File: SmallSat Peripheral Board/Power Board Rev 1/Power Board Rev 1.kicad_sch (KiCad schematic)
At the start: 41 parts, among them J1 Conn_01x02_Pin, J2 Conn_01x02_Pin, U1 DMN3020UFDF, U2 BQ296202DSGR, U3 DMN3020UFDF, U4 BQ28Z620DRZR, U5 TPS62993QRYTRQ1, U6 TPS62993QRYTRQ1

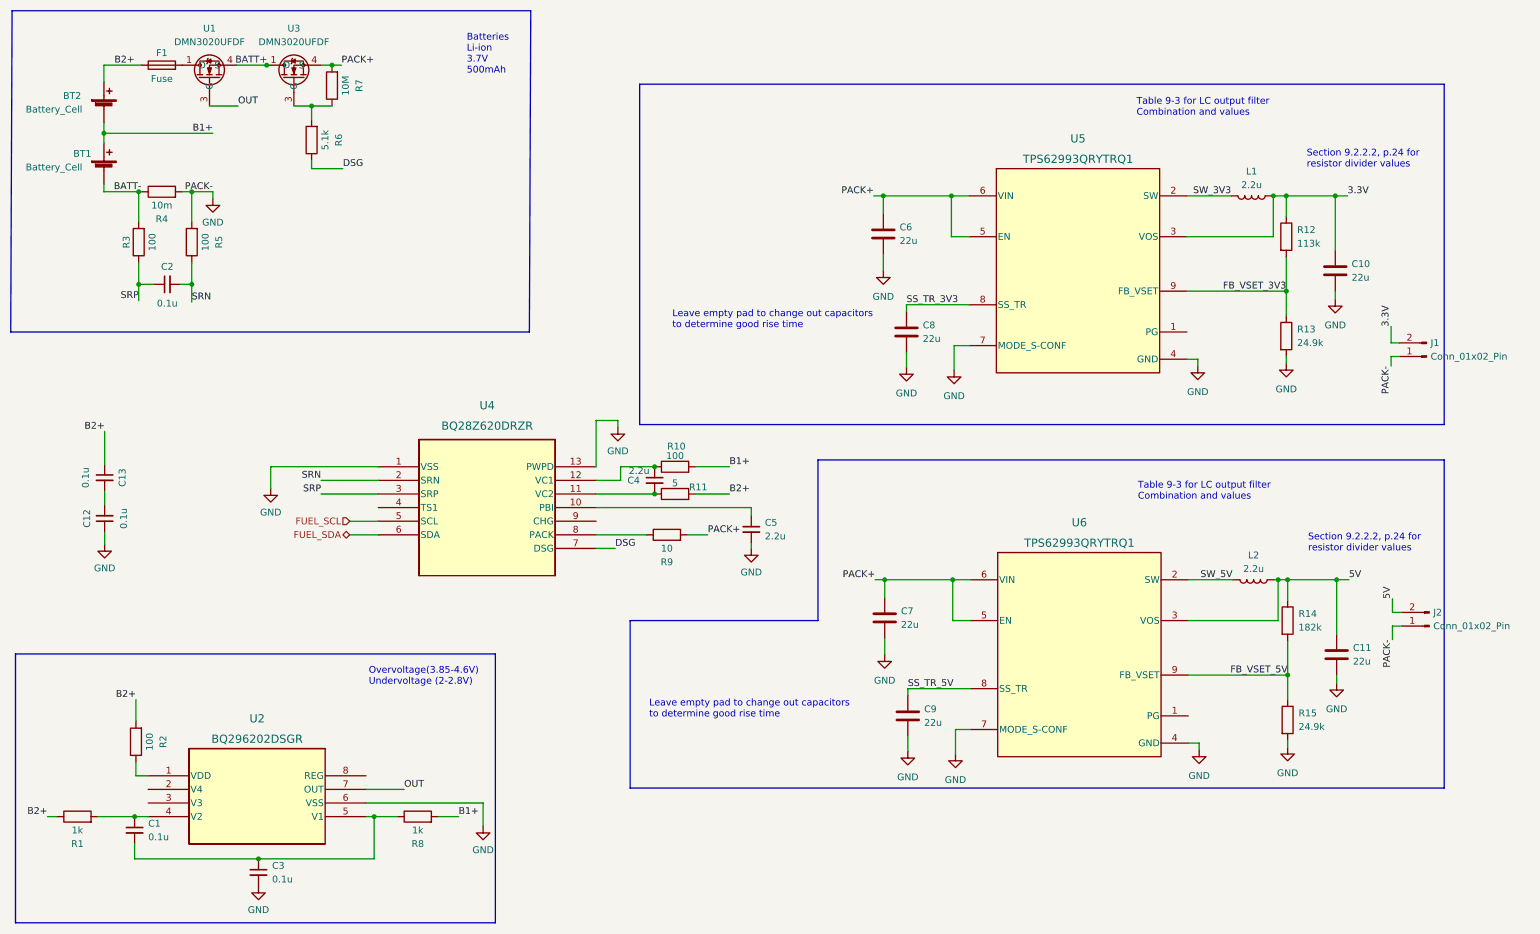
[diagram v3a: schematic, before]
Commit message: Power Board Rev 1 Gerber Files Generated
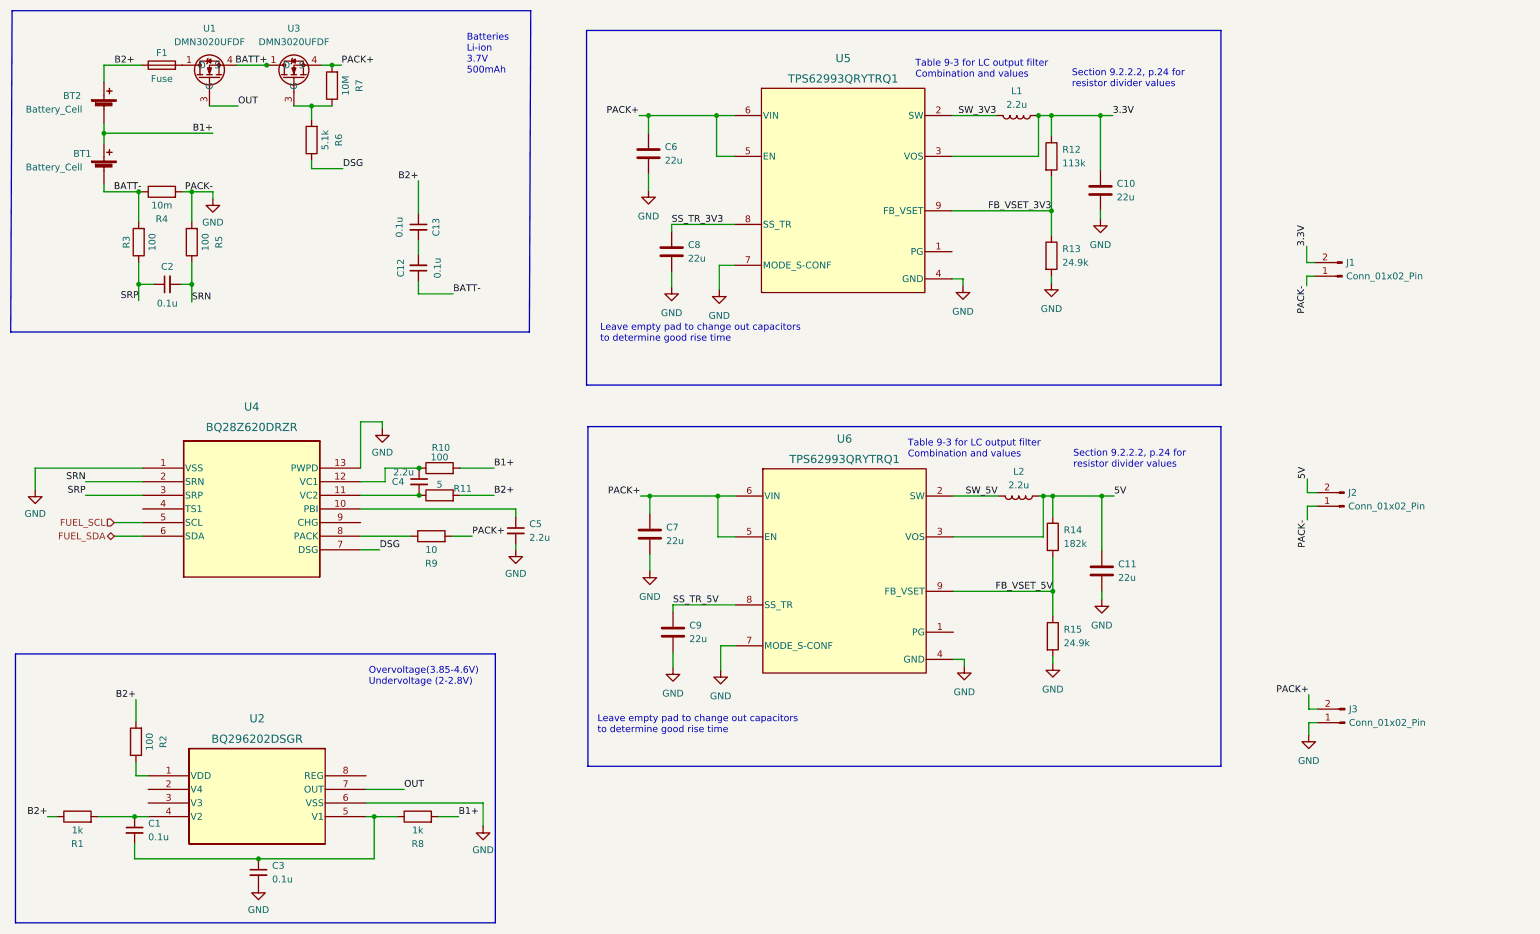
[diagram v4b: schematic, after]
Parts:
- added J3: Conn_01x02_Pin, Connector_PinSocket_1.00mm:PinSocket_1x02_P1.00mm_Vertical, symbol Connector:Conn_01x02_Pin
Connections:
- net BATT-: now also C12.1
- net GND: now also J3.1 (Pin_1); no longer C12.1
- net PACK+: now also J3.2 (Pin_2)
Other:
- moved on the sheet: C10, C11, C12, C13, C4, C5, C6, C7, C8, C9, J1, J2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

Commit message: PB-order version
Sent the order in for Rev 1 power board with this version
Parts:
- removed C10, C11, C6, C7, C8, C9: 22u, Capacitor_SMD:C_0402_1005Metric, symbol Device:C
- removed L1, L2: 2.2u, Inductor_SMD:L_1206_3216Metric, symbol Device:L
- removed R12: 113k, Resistor_SMD:R_0402_1005Metric, symbol Device:R
- removed R13, R15: 24.9k, Resistor_SMD:R_0402_1005Metric, symbol Device:R
- removed R14: 182k, Resistor_SMD:R_0402_1005Metric, symbol Device:R
- removed U5, U6: TPS62993QRYTRQ1, PowerBoardLibrary:RYT0009A-MFG, symbol SmallSat-Peripherals-Board:TPS62993QRYTRQ1
- added J4: Conn_01x02_Pin, Connector_PinSocket_1.00mm:PinSocket_1x02_P1.00mm_Vertical, symbol Connector:Conn_01x02_Pin
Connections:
- net FUEL_SCL renamed Fuel_SCL
- net Fuel_SCL: now also J4.1 (Pin_1)
- net FUEL_SDA renamed Fuel_SDA
- net Fuel_SDA: now also J4.2 (Pin_2)
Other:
- added sheet V_Regulation (V_Regulation.kicad_sch)
- note added: "Battery ESD Protection"
- note removed: "Leave empty pad to change out capacitors to determine good rise time"
- note removed: "Section 9.2.2.2, p.24 for resistor divider values"
- note removed: "Table 9-3 for LC output filter Combination and values"
- moved on the sheet: J1, J2, J3
